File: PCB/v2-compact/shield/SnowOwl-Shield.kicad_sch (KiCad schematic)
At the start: 0 parts

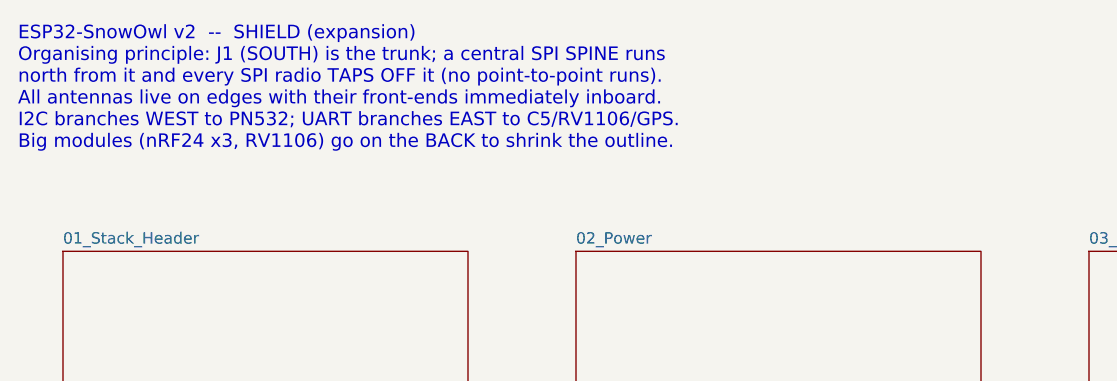
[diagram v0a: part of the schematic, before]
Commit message: PCB: rework main board to phone-style layout; J1 -> horizontal strip
Main board (per feedback) is now a phone-style split — front is pure UI, back
carries the electronics:
- FRONT: status LEDs at the very top (above the display), TFT rotated to
  LANDSCAPE (sideways), nav buttons below it and moved down. Same feel as the
  ESP32-DIV, sideways screen.
- BACK: ESP32-S3 behind the display, microSD beside it, power + USB-C at the
  bottom-centre edge like a phone.

To keep the centre column free for the landscape display and the bottom-centre
USB-C, J1 is reoriented from a vertical 2x10 to a HORIZONTAL 10x2 strip in the
lower-centre. J1 is the shared mating datum, so the shield's J1 moves to match;
the shield's RV1106 / HTRC110 / bulk-cap zones shift to sit above/below the new
strip (SPI spine still runs north from it). Every v1 capability unchanged.

Updated both .kicad_pcb, both floorplan SVGs, both schematics' zone specs, and
PLACEMENT.md. Verified: files parse, J1 clears all zones, no same-side overlaps.

Co-Authored-By: Claude <noreply@anthropic.com>
Claude-Session: https://claude.ai/code/session_017BEAKBRVwbUCc7Sa2o3Ye7
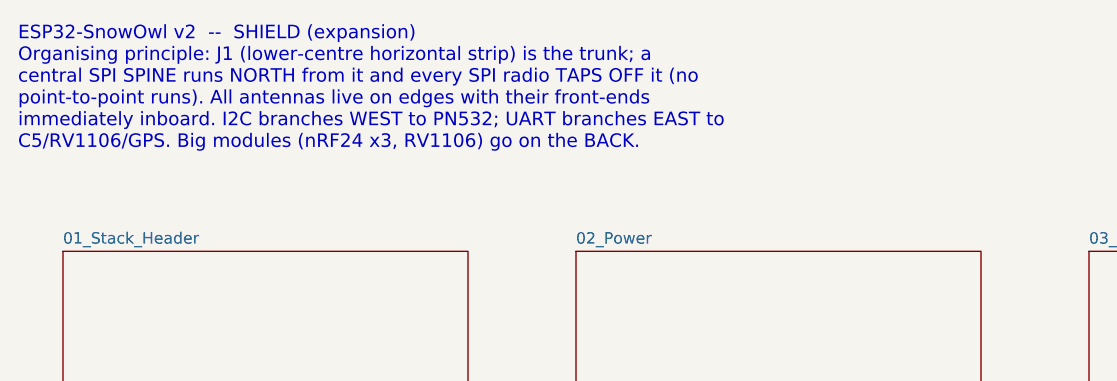
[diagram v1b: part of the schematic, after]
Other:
- note added: "ESP32-SnowOwl v2 -- SHIELD (expansion) Organising principle: J1 (lower-centre horizontal strip) is the trunk; a central SPI SPINE runs NORTH from it and every SPI radio TAPS OFF it (no point-to-point runs). All antennas live on edges with their front-ends immediately inboard. I2C branches WEST to PN532; UART branches EAST to C5/RV1106/GPS. Big modules (nRF24 x3, RV1106) go on the BACK."
- note removed: "ESP32-SnowOwl v2 -- SHIELD (expansion) Organising principle: J1 (SOUTH) is the trunk; a central SPI SPINE runs north from it and every SPI radio TAPS OFF it (no point-to-point runs). All antennas live on edges with their front-ends immediately inboard. I2C branches WEST to PN532; UART branches EAST to C5/RV1106/GPS. Big modules (nRF24 x3, RV1106) go on the BACK to shrink the outline."
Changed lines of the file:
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@@
     (comment 1 "ESP32-SnowOwl v2 - compact 2-board stack"))
   (text "ESP32-SnowOwl v2  --  SHIELD (expansion)
-Organising principle: J1 (SOUTH) is the trunk; a central SPI SPINE runs
-north from it and every SPI radio TAPS OFF it (no point-to-point runs).
-All antennas live on edges with their front-ends immediately inboard.
-I2C branches WEST to PN532; UART branches EAST to C5/RV1106/GPS.
-Big modules (nRF24 x3, RV1106) go on the BACK to shrink the outline." (at 20 15 0)
+Organising principle: J1 (lower-centre horizontal strip) is the trunk; a
+central SPI SPINE runs NORTH from it and every SPI radio TAPS OFF it (no
+point-to-point runs). All antennas live on edges with their front-ends
+immediately inboard. I2C branches WEST to PN532; UART branches EAST to
+C5/RV1106/GPS. Big modules (nRF24 x3, RV1106) go on the BACK." (at 20 15 0)
     (effects (font (size 1.5 1.5)) (justify left top)))
   (sheet (at 25.0 40.0) (size 45.0 24.0) (fields_autoplaced)
@@
   (sheet_instances
     (path "/" (page "1"))
-    (path "/7b3e1a98-f527-4213-84c0-74d89846ee26" (page "2"))
-    (path "/904ba787-71ec-465f-a120-3af7d50968a3" (page "3"))
-    (path "/b3fc31a6-bc86-4382-8a0d-924da81aa3d7" (page "4"))
-    (path "/ee19ddbe-5b08-42d8-8c27-950c80599492" (page "5"))
-    (path "/d3481d1f-f7dd-4ed0-b5a4-772344cfbeb9" (page "6"))
-    (path "/32943a2d-3f43-4ce2-b736-c69cee7e8302" (page "7"))
-    (path "/19bf8e43-84d2-4e55-beaa-91056c8a5568" (page "8"))
-    (path "/f4a2a3ce-c726-4fbb-be7d-49978f57c814" (page "9"))
-    (path "/80b273cb-d587-4a5c-849a-7beb2f2a02ae" (page "10"))
-    (path "/22b19b25-f2ba-4667-90f9-a5ce2f070736" (page "11"))
-    (path "/b02e19fb-bc00-4305-9b23-9afa0fa0fcc1" (page "12"))
-    (path "/06c1b2c8-aa1d-4f4f-9bc0-efad64877105" (page "13"))
+    (path "/2514f9b2-fc51-4408-b91e-9fbba2ba8e01" (page "2"))
+    (path "/494a1962-6497-488c-92c7-43459044dd8c" (page "3"))
+    (path "/777ab629-c829-4b4c-ac89-f132d977e771" (page "4"))
+    (path "/a336091c-7cef-45b2-8e8f-0835e68f0acf" (page "5"))
+    (path "/59e2d0d6-e793-4a43-bccb-69371ace0260" (page "6"))
+    (path "/1a2a1521-c839-4d6a-ad78-ab839713699a" (page "7"))
+    (path "/2c96ae28-ab46-4a33-bbca-ff7c9b41038c" (page "8"))
+    (path "/44195f86-bade-400a-b1c6-65bd4a325d72" (page "9"))
+    (path "/0a27d683-2113-42a8-9290-a545f7865850" (page "10"))
+    (path "/bf6bb016-fb66-45f6-916d-e11e6b4a930d" (page "11"))
+    (path "/76ddc4c2-3c0b-4070-9054-b9b062b12a9d" (page "12"))
+    (path "/4e94e7f7-7328-40c5-88b8-5d45dab38b09" (page "13"))
   )
 )
